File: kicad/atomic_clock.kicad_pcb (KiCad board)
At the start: 2 copper layers, 280.9 x 19.2 mm, 34 parts, among them J1 Conn_02x05_Top_Bottom, J10 Conn_02x05_Top_Bottom, J11 Conn_02x05_Top_Bottom, J2 Conn_02x05_Top_Bottom, J3 Conn_02x05_Top_Bottom, J4 Conn_02x05_Top_Bottom, J5 USB_B_Micro, J6 Conn_02x05_Top_Bottom, J7 Conn_02x05_Top_Bottom, J8 Conn_02x05_Top_Bottom, J9 Conn_02x05_Top_Bottom, U1 D198K, U10 ATSAMDA1E16B-A, U11 D198K, U12 D198K, U13 D198K, U14 D198K, U15 D198K, U16 MAX7221xWG, U17 D198K, U18 D198K, U19 D198K, U2 D198K, U3 D198K, U4 D198K, U5 MAX7221xWG, U6 D198K, U7 D198K, U8 D198K, U9 D198K

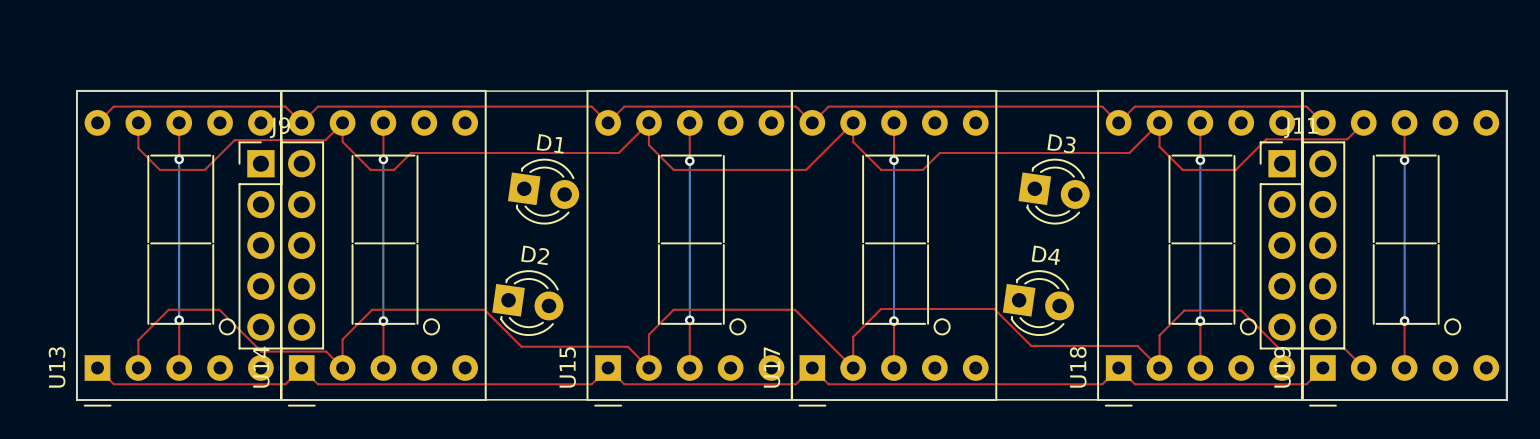
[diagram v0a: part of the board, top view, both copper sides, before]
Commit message: Lay out part of PCB
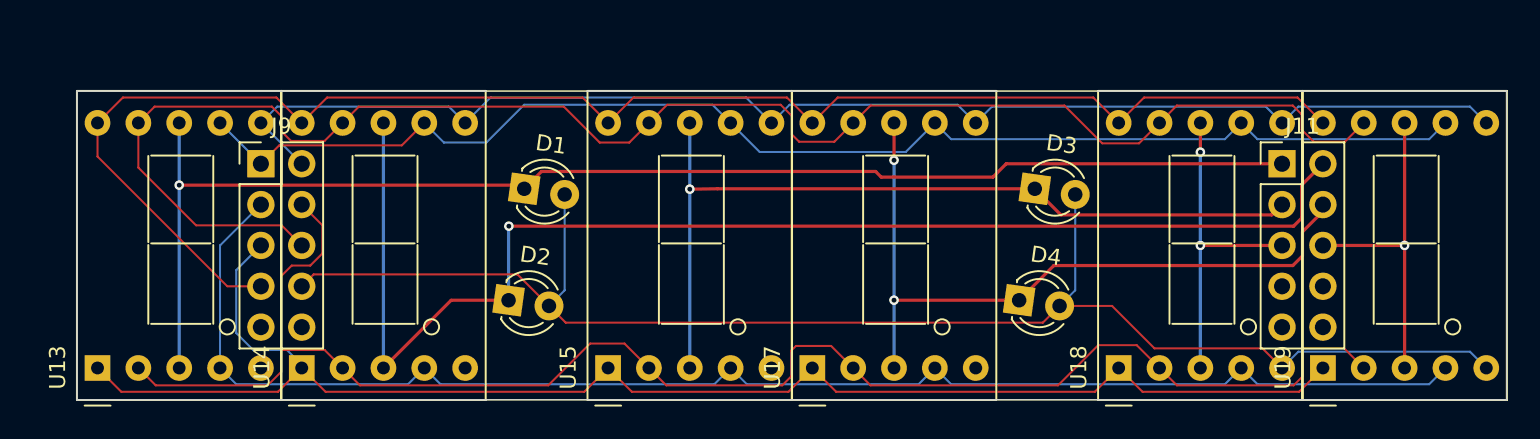
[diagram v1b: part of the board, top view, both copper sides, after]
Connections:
- D2 pad 1: /seg11 -> /3s11
- D4 pad 1: /seg13 -> /3s13
- J10 pad 1: /3s10 -> /1s10
- J10 pad 2: /3s11 -> /1s11
- J10 pad 3: /3s12 -> /1s12
- J10 pad 4: /3s13 -> /1s13
- J10 pad 5: /3s14 -> /1s14
- J10 pad 6: /3s15 -> /1s15
- U17 pad 3: /seg13 -> /3s13
- U17 pad 8: /seg13 -> /3s13
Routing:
- net /3DP2: track 0.00 -> 92.7 mm
- net /3C2: track 0.00 -> 91.6 mm
- net /3B2: track 0.00 -> 84.6 mm
- net /3A2: track 0.00 -> 83.4 mm
- net /3s10: track 15.2 -> 84.8 mm, vias 2 -> 1
- net /3s11: track 15.2 -> 82.8 mm, vias 2 -> 1
- net /3s13: track 0.00 -> 45.5 mm, vias 0 -> 2
- net /3s12: track 15.2 -> 53.0 mm, vias 2 -> 1
- net /3G2: track 80.4 -> 98.3 mm
- net /seg13: track 15.2 -> 0.00 mm, vias 2 -> 0
- net /3E2: track 80.4 -> 93.5 mm
- net /3F2: track 92.3 -> 102.3 mm
- net /3s15: track 15.2 -> 20.3 mm, vias 2 -> 1
- net /3s14: track 15.2 -> 20.3 mm
- net /3D2: track 96.8 -> 100.2 mm

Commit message: Progress on PCB
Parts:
- added C1: 100nF, Capacitor_SMD:C_0805_2012Metric, B.Cu at (46.1, 115.0)
- added C2: 10uF, Capacitor_SMD:C_0805_2012Metric, B.Cu at (127.7, 116.0)
- added C3: 10uF, Capacitor_SMD:C_0805_2012Metric, B.Cu at (131.8, 110.0)
- added C4: C, Capacitor_SMD:C_0805_2012Metric, B.Cu at (108.3, 123.6)
- added C5: C, Capacitor_SMD:C_0805_2012Metric, B.Cu at (109.7, 122.1)
- added C6: 100nF, Capacitor_SMD:C_0805_2012Metric, B.Cu at (111.2, 120.7)
- added C7: 100nF, Capacitor_SMD:C_0805_2012Metric, B.Cu at (263.8, 115.8)
- added J12: USB_B_Micro, Connector_USB:USB_Micro-B_Amphenol_10118194_Horizontal, B.Cu at (163.2, 123.0)
- added J13: Conn_ARM_JTAG_SWD_10, local_footprints:sam_swd_header, B.Cu at (124.2, 122.7)
- added J14: Conn_01x03_Female, Connector_PinSocket_2.54mm:PinSocket_1x03_P2.54mm_Vertical, B.Cu at (113.8, 109.2)
- added R1: 10K, Resistor_SMD:R_0805_2012Metric, B.Cu at (46.1, 117.1)
- added R2: 1K, Resistor_SMD:R_0805_2012Metric, B.Cu at (117.2, 123.8)
- added R3: 10K, Resistor_SMD:R_0805_2012Metric, B.Cu at (131.1, 123.8)
- added R4: 10K, Resistor_SMD:R_0805_2012Metric, B.Cu at (263.8, 117.9)
- added U20: NCP1117LPST33T3G, Package_TO_SOT_SMD:SOT-223, B.Cu at (125.5, 110.9)
- added U21: mems_osc_st1630, Package_TO_SOT_SMD:SOT-23-5, B.Cu at (99.4, 123.0)
- J5: footprint Connector_USB:USB_Micro-B_Amphenol_10118194_Horizontal -> Connector_USB:USB_Micro-B_Molex-105133-0001; moved to B.Cu
- U10, U16, U5: moved to B.Cu
- moved J3 175.6 mm to (85.0, 111.1)
- moved J10 147.0 mm to (289.7, 111.1)
- moved J8 123.7 mm to (226.2, 111.1)
- moved J6 119.4 mm to (135.8, 111.1)
- moved J1 96.9 mm to (34.2, 111.1)
- moved U10 80.8 mm to (104.2, 116.6), turned to 45 degrees
- moved J5 72.0 mm to (154.1, 122.6), turned to 180 degrees
- moved U16 53.8 mm to (272.1, 116.5), turned to 180 degrees
- moved U5 46.5 mm to (54.1, 116.1), turned to 180 degrees
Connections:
- J5 pad 6: unconnected-(J5-Pad6) -> GND
- U10 pad 1: unconnected-(U10-Pad1) -> /XIN32
- U10 pad 11: unconnected-(U10-Pad11) -> Net-(U10-Pad11)
- U10 pad 12: unconnected-(U10-Pad12) -> Net-(U10-Pad12)
- U10 pad 13: unconnected-(U10-Pad13) -> Net-(U10-Pad13)
- U10 pad 14: unconnected-(U10-Pad14) -> Net-(U10-Pad14)
- U10 pad 26: unconnected-(U10-Pad26) -> Net-(C6-Pad1)
- U10 pad 29: /5V -> Net-(C5-Pad1)
- U10 pad 30: /5V -> /3.3V
- U10 pad 31: unconnected-(U10-Pad31) -> /SWCLK
- U10 pad 32: unconnected-(U10-Pad32) -> /SWDIO
- U10 pad 9: /5V -> /3.3V
- U16 pad 1: unconnected-(U16-Pad1) -> Net-(U16-Pad1)
- U16 pad 12: unconnected-(U16-Pad12) -> Net-(U10-Pad14)
- U16 pad 13: unconnected-(U16-Pad13) -> Net-(U10-Pad12)
- U16 pad 18: unconnected-(U16-Pad18) -> Net-(R4-Pad1)
- U5 pad 1: unconnected-(U5-Pad1) -> Net-(U10-Pad11)
- U5 pad 12: unconnected-(U5-Pad12) -> Net-(U10-Pad13)
- U5 pad 13: unconnected-(U5-Pad13) -> Net-(U10-Pad12)
- U5 pad 18: unconnected-(U5-Pad18) -> Net-(R1-Pad1)
- U5 pad 24: unconnected-(U5-Pad24) -> Net-(U16-Pad1)
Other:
- board size 280.9 x 19.2 mm -> 280.9 x 44.4 mm

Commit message: Layout mostly done.
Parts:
- added C8: 100nF, Capacitor_SMD:C_0805_2012Metric, B.Cu at (81.9, 108.7)
- added R5: 10K, Resistor_SMD:R_0805_2012Metric, B.Cu at (148.4, 109.0)
- added R6: R_Photo, OptoDevice:R_LDR_4.9x4.2mm_P2.54mm_Vertical, F.Cu at (151.7, 109.0)
- added U22: DHT20, local_footprints:DHT20, B.Cu at (80.7, 112.4)
- added U23: DCF77, local_footprints:DCF77 receiver module, B.Cu at (259.2, 109.4)
- moved C1 1.78 mm to (44.3, 115.0)
- moved R1 1.78 mm to (44.3, 117.1)
- moved U5 1.78 mm to (52.3, 116.1)
- moved J5 0.79 mm to (154.1, 123.4)
- moved C4 0.46 mm to (108.4, 123.1)
- moved C5 0.46 mm to (109.8, 121.7)
- moved C6 0.46 mm to (111.3, 120.2)
- moved U10 0.40 mm to (104.2, 116.2)
- moved J12 0.11 mm to (163.2, 122.9)
- moved U21 0.05 mm to (99.4, 123.0)
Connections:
- net Net-(U10-Pad11) renamed /DO
- net Net-(U10-Pad12) renamed /SCK
- J12 pad 1: /5V -> Net-(J12-Pad1)
- J5 pad 1: /5V -> Net-(J5-Pad1)
- U10 pad 13: Net-(U10-Pad13) -> /~SS
- U10 pad 14: Net-(U10-Pad14) -> unconnected-(U10-Pad14)
- U10 pad 17: unconnected-(U10-Pad17) -> Net-(U22-Pad2)
- U10 pad 18: unconnected-(U10-Pad18) -> Net-(U22-Pad4)
- U10 pad 21: unconnected-(U10-Pad21) -> /DCF_DATA
- U10 pad 22: unconnected-(U10-Pad22) -> /DCF_PDN
- U10 pad 23: unconnected-(U10-Pad23) -> /USB-
- U10 pad 24: /USB- -> /USB+
- U10 pad 25: /USB+ -> /LDR_SINK
- U10 pad 3: unconnected-(U10-Pad3) -> /LDR
- U10 pad 4: /UART_TX -> unconnected-(U10-Pad4)
- U10 pad 5: /UART_RX -> /UART_TX
- U10 pad 7: unconnected-(U10-Pad7) -> /UART_RX
- U16 pad 12: Net-(U10-Pad14) -> /~SS
- U5 pad 12: Net-(U10-Pad13) -> /~SS
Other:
- board size 280.9 x 44.4 mm -> 280.9 x 44.3 mm
- board text added: "Ferrite core antenna"
- board text added: "GND"
- board text added: "RX"
- board text added: "TX"

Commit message: Stretch PCB to accommodate the LDR.
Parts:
- added D5: D, Diode_SMD:D_SMA, B.Cu at (164.1, 115.7)
- added D6: D, Diode_SMD:D_SMA, B.Cu at (154.1, 115.7)
- moved R5 65.7 mm to (214.0, 112.5)
- moved R6 61.0 mm to (212.7, 109.1)
- moved C7 2.00 mm to (265.8, 115.8)
- moved D1 2.00 mm to (244.5, 87.5)
- moved D2 2.00 mm to (243.6, 94.4)
- moved D3 2.00 mm to (276.3, 87.5)
- moved D4 2.00 mm to (275.3, 94.4)
- moved J10 2.00 mm to (291.7, 111.1)
- moved J11 2.00 mm to (291.7, 85.9)
- moved J8 2.00 mm to (228.2, 111.1)
- moved J9 2.00 mm to (228.2, 85.9)
- moved R4 2.00 mm to (265.8, 117.9)
- moved U13 2.00 mm to (218.0, 98.6)
- moved U14 2.00 mm to (230.7, 98.6)
- moved U15 2.00 mm to (249.8, 98.6)
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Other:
- board size 280.9 x 44.3 mm -> 282.9 x 44.2 mm

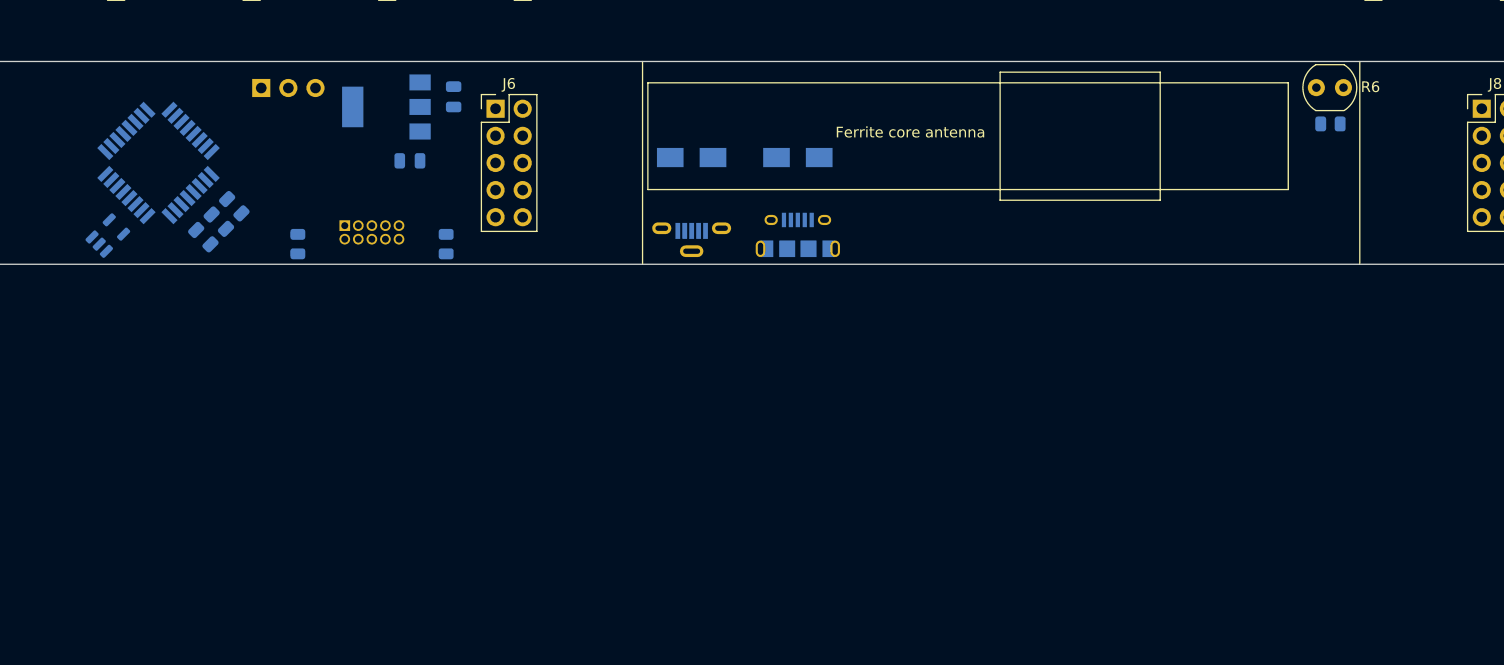
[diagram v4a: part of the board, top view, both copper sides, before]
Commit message: Reworked battery/power system
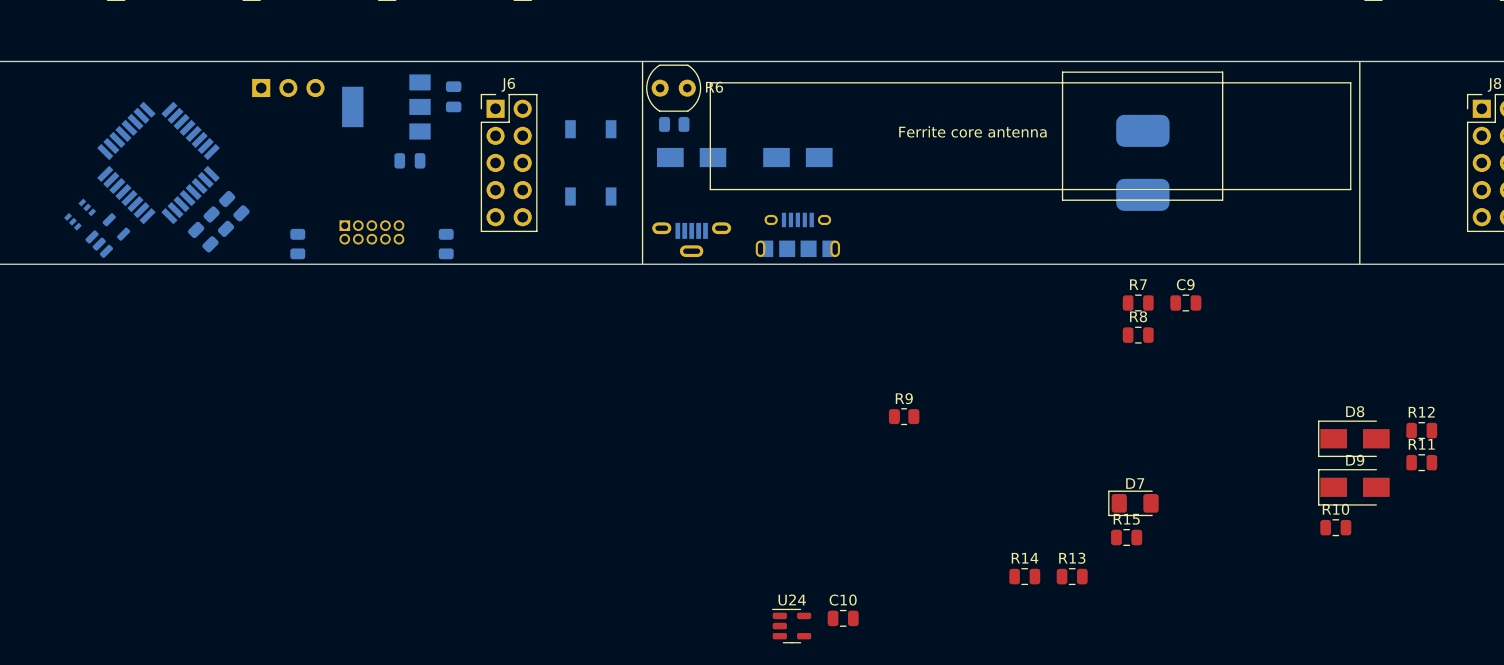
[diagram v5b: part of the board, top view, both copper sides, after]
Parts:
- added BT1: Battery_Cell, local_footprints:Battery_pads, B.Cu at (196.4, 116.2)
- added C10: 4.7uF, Capacitor_SMD:C_0805_2012Metric, F.Cu at (168.3, 158.9)
- added C9: 4.7uF, Capacitor_SMD:C_0805_2012Metric, F.Cu at (200.4, 129.3)
- added D7: LED, LED_SMD:LED_1206_3216Metric_Pad1.42x1.75mm_HandSolder, F.Cu at (195.7, 148.1)
- added D8: D, Diode_SMD:D_SMA, F.Cu at (216.3, 142.0)
- added D9: D, Diode_SMD:D_SMA, F.Cu at (216.3, 146.6)
- added Q1: Q_Dual_PMOS_S1G1D2S2G2D1, Package_TO_SOT_SMD:SOT-363_SC-70-6, B.Cu at (96.8, 121.0)
- added R10: 10K, Capacitor_SMD:C_0805_2012Metric, F.Cu at (214.5, 150.4)
- added R11: 10K, Capacitor_SMD:C_0805_2012Metric, F.Cu at (222.5, 144.3)
- added R12: 10K, Capacitor_SMD:C_0805_2012Metric, F.Cu at (222.5, 141.3)
- added R13: 10K, Capacitor_SMD:C_0805_2012Metric, F.Cu at (189.8, 154.9)
- added R14: 10K, Capacitor_SMD:C_0805_2012Metric, F.Cu at (185.3, 154.9)
- added R15: 10K, Capacitor_SMD:C_0805_2012Metric, F.Cu at (194.9, 151.3)
- added R7: 10K, Capacitor_SMD:C_0805_2012Metric, F.Cu at (196.0, 129.3)
- added R8: 330R, Capacitor_SMD:C_0805_2012Metric, F.Cu at (196.0, 132.3)
- added R9: 10K, Resistor_SMD:R_0805_2012Metric, F.Cu at (174.0, 139.9)
- added SW1: SW_Push, Button_Switch_SMD:SW_SPST_TL3342, B.Cu at (144.7, 116.2)
- added U24: MCP73831-2-OT, Package_TO_SOT_SMD:SOT-23-5, F.Cu at (163.5, 159.6)
- moved R5 61.5 mm to (152.5, 112.6)
- moved R6 61.5 mm to (151.2, 109.2)
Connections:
- net /~SS renamed /~{SS}
- C2 pad 1: /5V -> Net-(C2-Pad1)
- C8 pad 1: /3.3V -> /3.3V_peripherals
- U10 pad 16: unconnected-(U10-Pad16) -> /SWITCH
- U10 pad 21: /DCF_DATA -> /UART_TX
- U10 pad 22: /DCF_PDN -> /UART_RX
- U10 pad 5: /UART_TX -> /~{peripheral_ctrl}
- U10 pad 6: unconnected-(U10-Pad6) -> /pwr_sense
- U10 pad 7: /UART_RX -> /DCF_DATA
- U10 pad 8: unconnected-(U10-Pad8) -> /DCF_PDN
- U20 pad 3: /5V -> Net-(C2-Pad1)
- U22 pad 1: /3.3V -> /3.3V_peripherals
- U23 pad 1: /3.3V -> /3.3V_peripherals
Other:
- board text added: "25mA @ 4.2v Charge current"
- board text added: "CP1654 Coin cell"
- board text added: "Rechargeable LiPo only!"

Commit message: Finished PCB placement
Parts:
- added Q2: Q_Dual_PMOS, Package_TO_SOT_SMD:SOT-363_SC-70-6, B.Cu at (147.2, 115.7)
- added U25: TXB0101, Package_TO_SOT_SMD:SOT-363_SC-70-6, B.Cu at (143.6, 115.7)
- C10, C9, D7, D8, D9, R9, U24: moved to B.Cu
- Q1: value Q_Dual_PMOS_S1G1D2S2G2D1 -> Q_Dual_PMOS
- R10, R11, R12, R13, R14, R15, R7, R8: footprint Capacitor_SMD:C_0805_2012Metric -> Resistor_SMD:R_0805_2012Metric; moved to B.Cu
- moved R12 104.3 mm to (120.7, 118.7), turned to 180 degrees
- moved R11 101.6 mm to (124.2, 118.7), turned to 180 degrees
- moved R10 92.4 mm to (127.7, 118.7), turned to 180 degrees
- moved U24 89.1 mm to (238.7, 111.8)
- moved C10 82.0 mm to (235.5, 111.8), turned to 90 degrees
- moved D9 76.7 mm to (143.6, 122.0), turned to -90 degrees
- moved D8 71.9 mm to (147.2, 122.0), turned to -90 degrees
- moved R9 71.3 mm to (110.4, 107.8), turned to 180 degrees
- moved R14 66.9 mm to (240.3, 116.8), turned to 180 degrees
- moved R13 62.0 mm to (240.3, 118.9), turned to 180 degrees
- moved R15 54.5 mm to (240.3, 121.0)
- moved D7 52.0 mm to (236.9, 116.3), turned to -90 degrees
- moved R7 46.6 mm to (240.3, 114.7)
- moved C9 45.1 mm to (242.0, 111.8), turned to -90 degrees
- moved R8 42.5 mm to (236.9, 120.6), turned to -90 degrees
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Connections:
- net /~{peripheral_ctrl} renamed /~{PERIPHERAL_CTL}
- C8 pad 1: /3.3V_peripherals -> /PERIPHERAL_PWR
- D5 pad 1: /5V -> Net-(D5-Pad1)
- D6 pad 1: /5V -> Net-(D5-Pad1)
- D8 pad 2: /5V -> Net-(D5-Pad1)
- Q1 pad 3: (no net) -> /3.3V_DCF
- Q1 pad 4: (no net) -> /3.3V
- Q1 pad 5: (no net) -> /~{DCF_CTL}
- Q1 pad 6: /3.3V_peripherals -> /PERIPHERAL_PWR
- R10 pad 1: /5V -> Net-(D5-Pad1)
- U10 pad 4: unconnected-(U10-Pad4) -> /~{DCF_CTL}
- U22 pad 1: /3.3V_peripherals -> /PERIPHERAL_PWR
- U23 pad 1: /3.3V_peripherals -> /3.3V_DCF
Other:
- outline, holes or cut-outs redrawn

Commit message: Start routing
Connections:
- net Net-(D5-Pad1) renamed /USB_PWR
- J10 pad 7: unconnected-(J10-Pad7) -> /1IND
- J11 pad 7: unconnected-(J11-Pad7) -> /3IND
- U10 pad 15: unconnected-(U10-Pad15) -> /1IND
- U19 pad 5: /3DP2 -> /3IND
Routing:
- net GND: track 0.00 -> 434.0 mm, vias 0 -> 13
- net /5V: track 0.00 -> 294.7 mm, vias 0 -> 5
- net /3.3V: track 0.00 -> 118.7 mm, vias 0 -> 9
- net /USB_PWR: track 0.00 -> 32.6 mm, vias 0 -> 2
- net /1s11: track 0.00 -> 23.5 mm
- net /1s13: track 0.00 -> 17.1 mm
- net /3IND: track 0.00 -> 14.8 mm
- net /1s10: track 0.00 -> 14.0 mm
- net /3DP2: track 92.7 -> 79.2 mm
- net /1s15: track 0.00 -> 9.63 mm
- net /1s14: track 0.00 -> 6.84 mm
- net /1s12: track 0.00 -> 6.84 mm
- net /SWITCH: track 0.00 -> 6.30 mm
- net /~{PERIPHERAL_CTL}: track 0.00 -> 3.99 mm
- net Net-(C2-Pad1): track 0.00 -> 3.60 mm
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
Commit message: Routed PCB
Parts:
- added R16: 220R, Resistor_SMD:R_0805_2012Metric, B.Cu at (298.0, 116.2)
- moved R9 6.66 mm to (103.7, 107.8)
- moved J14 0.65 mm to (97.7, 109.2)
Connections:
- net /USB+ renamed /USB_P
- net /USB- renamed /USB_N
- net Net-(C2-Pad1) renamed /NCP_IN
- U10 pad 15: /1IND -> Net-(R16-Pad1)
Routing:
- net /~{SS}: track 0.00 -> 287.4 mm, vias 0 -> 4
- net /SCK: track 0.00 -> 262.2 mm, vias 0 -> 4
- net Net-(U16-Pad1): track 0.00 -> 241.2 mm, vias 0 -> 2
- net /1s8: track 0.00 -> 227.2 mm, vias 0 -> 1
- net /1s9: track 0.00 -> 207.7 mm, vias 0 -> 1
- net Net-(R16-Pad1): track 0.00 -> 206.5 mm, vias 0 -> 2
- net /3.3V_DCF: track 0.00 -> 173.5 mm, vias 0 -> 1
- net /DCF_DATA: track 0.00 -> 161.7 mm, vias 0 -> 1
- net /DCF_PDN: track 0.00 -> 157.8 mm, vias 0 -> 1
- net /1B2: track 0.00 -> 154.0 mm, vias 0 -> 1
- net /1A2: track 0.00 -> 154.0 mm, vias 0 -> 2
- net /1DP2: track 0.00 -> 151.2 mm, vias 0 -> 3
- net /1F2: track 0.00 -> 150.8 mm, vias 0 -> 2
- net /1E2: track 0.00 -> 148.2 mm, vias 0 -> 2
- net /1G2: track 0.00 -> 145.4 mm, vias 0 -> 2
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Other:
- board text added: "UART"
